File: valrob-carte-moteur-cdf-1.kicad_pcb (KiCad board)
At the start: 2 copper layers, 63 x 50 mm, 85 parts, among them J1 USB_C_Receptacle_USB2.0_14P, J2 Conn_01x02, J3 Conn_01x02, J4 Conn_01x04_Pin, J5 Conn_01x08, J6 Conn_01x02, J7 Conn_01x02, J8 Conn_01x08, SW1 SW_Push, SW2 SW_Push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

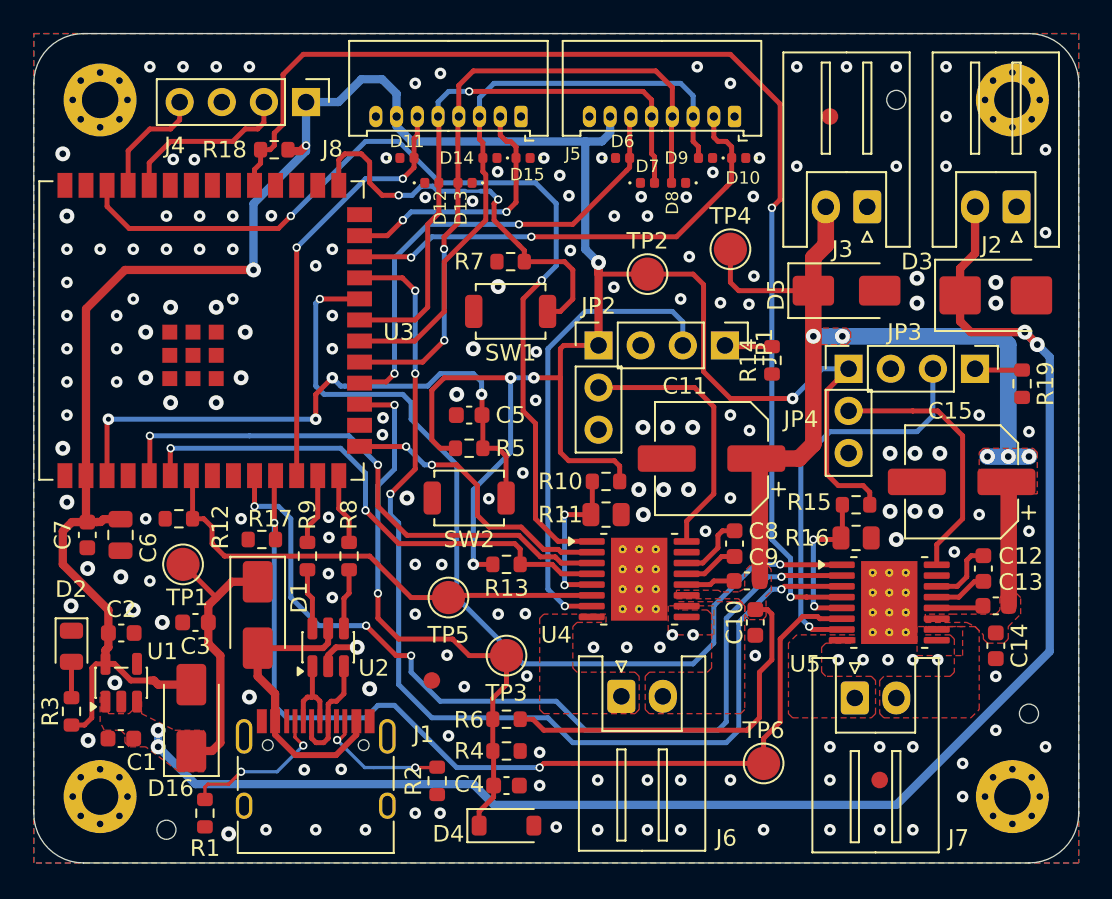
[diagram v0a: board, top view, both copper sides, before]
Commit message: pcb: add silkscreen bling
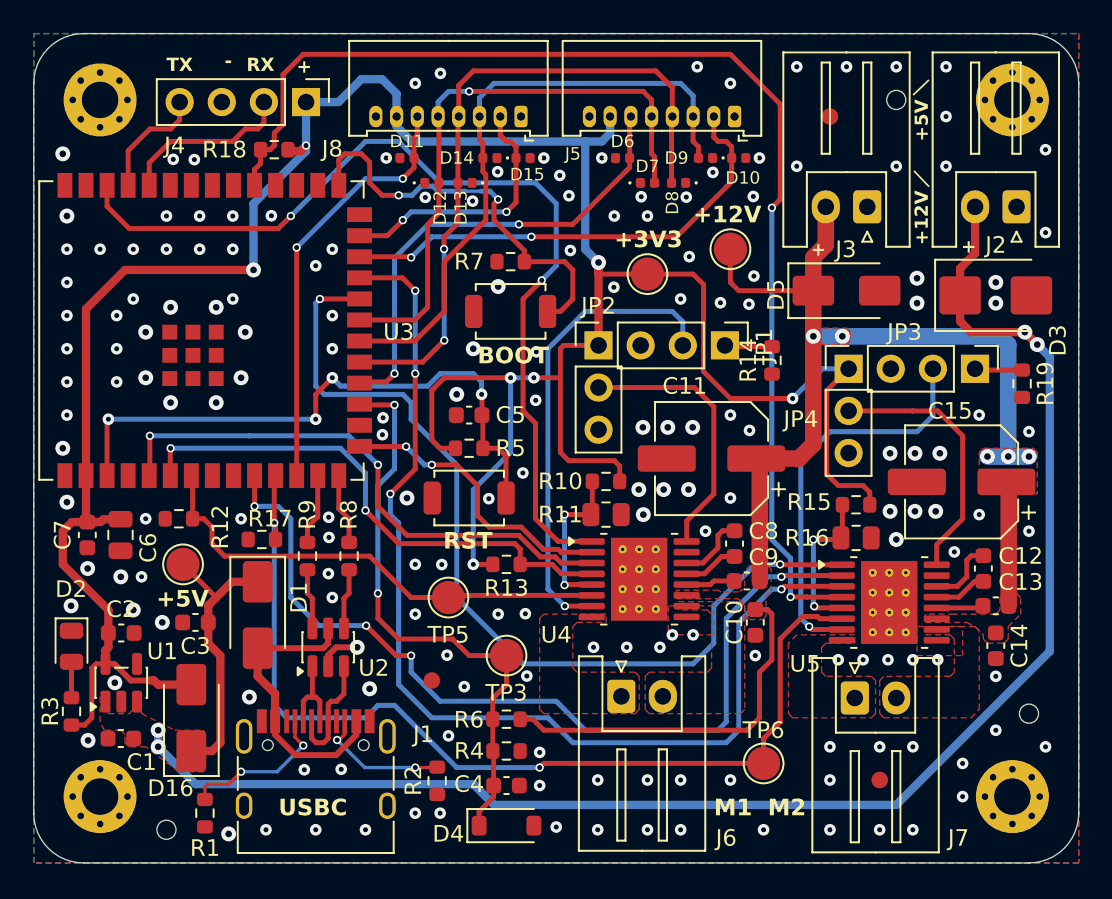
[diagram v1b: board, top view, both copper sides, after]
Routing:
- net GND: vias 183 -> 179
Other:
- board text added: "+"
- board text added: "+12V"
- board text added: "+3V3"
- board text added: "+5V"
- board text added: "-"
- board text added: ">10A"
- board text added: "ALERT1"
- board text added: "ALERT2"
- board text added: "BOOT"
- board text added: "CS0"
- board text added: "CS1"
- board text added: "Carte moteur CDF 1"
- board text added: "GND"
- board text added: "ICHOPPING"
- board text added: "M1"
- board text added: "M2"
- board text added: "MISO"
- board text added: "MOSI"
- board text added: "N"
- board text added: "PH/EN"
- board text added: "PWM"
- board text added: "RST"
- board text added: "RX"
- board text added: "Rev 01"
- board text added: "SCLK"
- board text added: "TX"
- board text added: "USBC"
- board text added: "Valrobotik 2025-11"
- board text added: "Y"

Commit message: add spare gpios
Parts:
- added J9: Conn_01x04_Pin, Connector_PinHeader_2.54mm:PinHeader_1x04_P2.54mm_Vertical, F.Cu at (99.4, 89.5)
- moved R18 29.4 mm to (126.8, 94.8), turned to -90 degrees
- moved J4 2.13 mm to (99.4, 87.0)
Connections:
- C5 pad 1: /CHIP_PU -> GND
- C5 pad 2: GND -> /CHIP_PU
- U3 pad 32: unconnected-(U3-MTCK/GPIO39/CLK_OUT3/SUBSPICS1-Pad32) -> Net-(J9-Pin_1)
- U3 pad 33: unconnected-(U3-MTDO/GPIO40/CLK_OUT2-Pad33) -> Net-(J9-Pin_2)
- U3 pad 34: unconnected-(U3-MTDI/GPIO41/CLK_OUT1-Pad34) -> Net-(J9-Pin_3)
- U3 pad 35: unconnected-(U3-MTMS/GPIO42-Pad35) -> Net-(J9-Pin_4)
- U4 pad 17: GND -> (no net)
- U5 pad 17: GND -> (no net)
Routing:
- net Net-(J9-Pin_1): track 0.00 -> 7.89 mm
- net Net-(J9-Pin_2): track 0.00 -> 6.63 mm
- net Net-(J9-Pin_3): track 0.00 -> 5.96 mm
- net Net-(J9-Pin_4): track 0.00 -> 4.84 mm
- net +3V3: track 169.4 -> 173.9 mm, vias 7 -> 6
- net /U0RXD: track 10.5 -> 12.7 mm
- net /U0TXD: track 7.04 -> 9.20 mm
- net /DC Driver 2/~{FAULT}: track 72.9 -> 72.2 mm
- net GND: vias 179 -> 177
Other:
- board text added: "39"
- board text added: "40"
- board text added: "41"
- board text added: "42"
- board text added: "ENCODER1"
- board text added: "ENCODER2"
- board text added: "GPIO"
- board text added: "UART"

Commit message: pcb(silkscreen): add JLC order number placeholder
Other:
- board text added: "JLCJLCJLCJLC"
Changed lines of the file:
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@@
+		)
+	)
+	(gr_text "JLCJLCJLCJLC"
+		(at 98.25 112.25 0)
+		(layer "B.SilkS")
+		(effects
+			(font
+				(size 1 1)
+				(thickness 0.1)
+			)
+			(justify left bottom mirror)
 		)
 	)

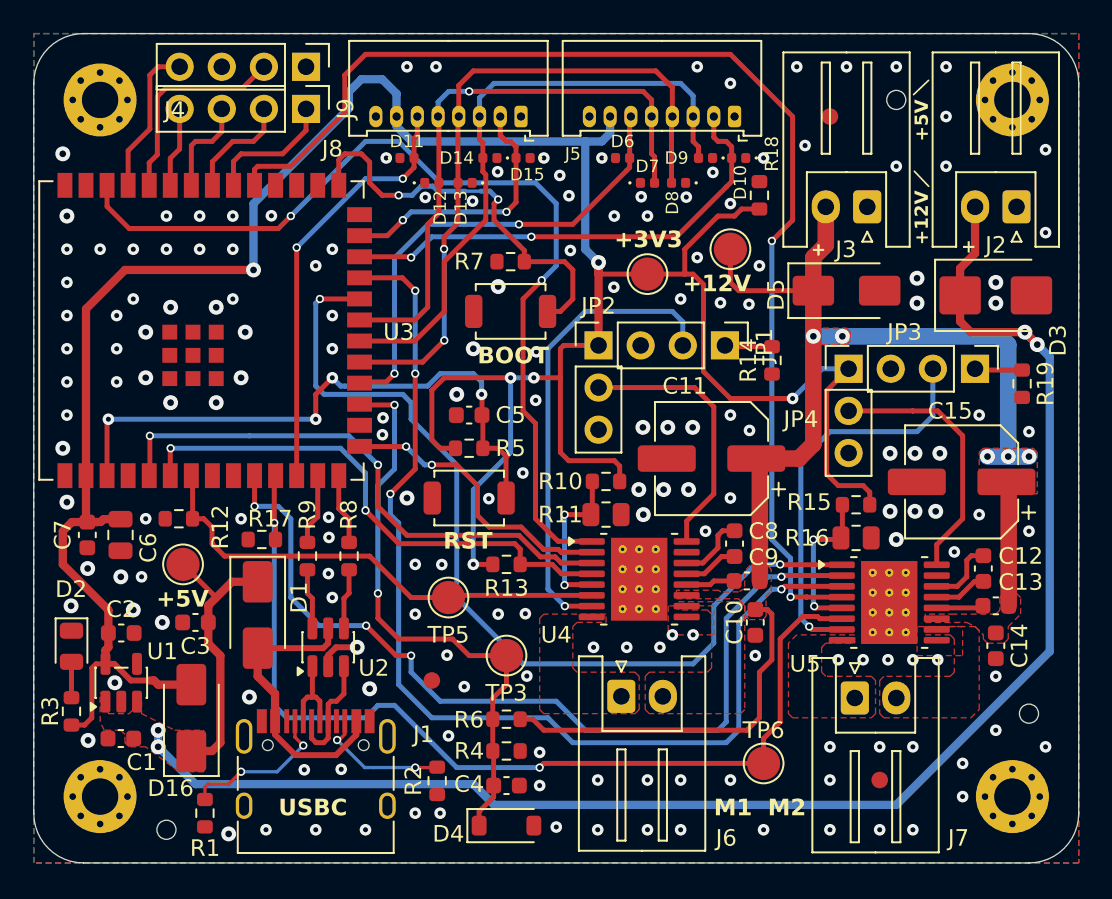
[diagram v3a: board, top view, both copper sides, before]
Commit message: pcb: run and fix DRC
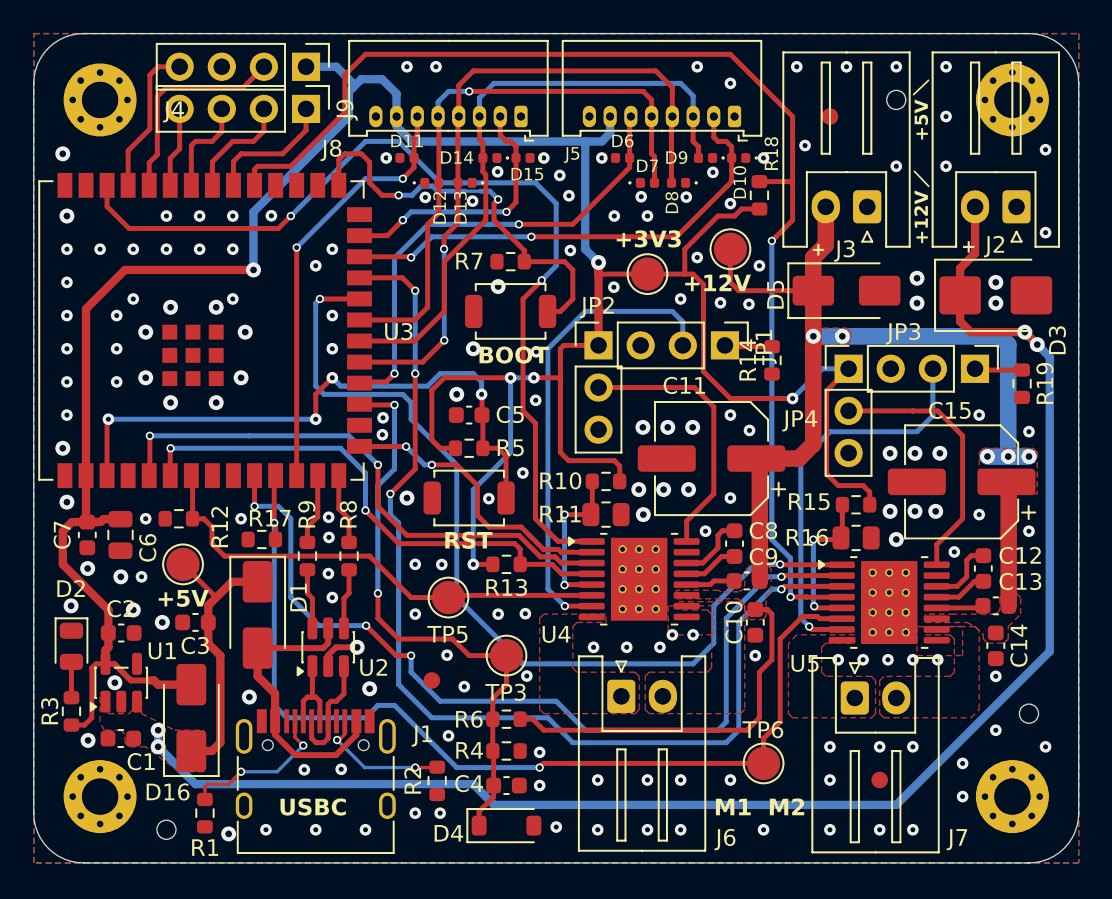
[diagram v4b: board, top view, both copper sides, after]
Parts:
- turned C5 to 0 degrees
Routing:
- net +3V3: track 173.9 -> 177.4 mm
- net /DC Driver 2/~{FAULT}: track 72.2 -> 74.2 mm
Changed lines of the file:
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@@
 			(at -1 -1.8)
 			(size 0.5 0.5)
-			(drill 0.2)
+			(drill 0.3)
 			(property pad_prop_heatsink)
 			(layers "*.Cu")
@@
 			(at -1 -0.6)
 			(size 0.5 0.5)
-			(drill 0.2)
+			(drill 0.3)
 			(property pad_prop_heatsink)
 			(layers "*.Cu")
@@
 			(at -1 0.6)
 			(size 0.5 0.5)
-			(drill 0.2)
+			(drill 0.3)
 			(property pad_prop_heatsink)
 			(layers "*.Cu")
@@
 			(at -1 1.8)
 			(size 0.5 0.5)
-			(drill 0.2)
+			(drill 0.3)
 			(property pad_prop_heatsink)
 			(layers "*.Cu")
@@
 			(at 0 -1.8)
 			(size 0.5 0.5)
-			(drill 0.2)
+			(drill 0.3)
 			(property pad_prop_heatsink)
 			(layers "*.Cu")
@@
 			(at 0 -0.6)
 			(size 0.5 0.5)
-			(drill 0.2)
+			(drill 0.3)
 			(property pad_prop_heatsink)
 			(layers "*.Cu")
@@
 			(at 0 0.6)
 			(size 0.5 0.5)
-			(drill 0.2)
+			(drill 0.3)
 			(property pad_prop_heatsink)
 			(layers "*.Cu")
@@
 			(at 0 1.8)
 			(size 0.5 0.5)
-			(drill 0.2)
+			(drill 0.3)
 			(property pad_prop_heatsink)
 			(layers "*.Cu")
@@
 			(at 1 -1.8)
 			(size 0.5 0.5)
-			(drill 0.2)
+			(drill 0.3)
 			(property pad_prop_heatsink)
 			(layers "*.Cu")
@@
 			(at 1 -0.6)
 			(size 0.5 0.5)
-			(drill 0.2)
+			(drill 0.3)
 			(property pad_prop_heatsink)
 			(layers "*.Cu")
@@
 			(at 1 0.6)
 			(size 0.5 0.5)
-			(drill 0.2)
+			(drill 0.3)
 			(property pad_prop_heatsink)
 			(layers "*.Cu")
@@
 			(at 1 1.8)
 			(size 0.5 0.5)
-			(drill 0.2)
+			(drill 0.3)
 			(property pad_prop_heatsink)
 			(layers "*.Cu")
@@
 		(tags "Diode SMA (DO-214AC)")
 		(property "Reference" "D16"
-			(at -4.25 -1.25 180)
+			(at -4.508165 -1.426515 180)
 			(layer "F.SilkS")
 			(effects
@@
 			(at -1 -1.8)
 			(size 0.5 0.5)
-			(drill 0.2)
+			(drill 0.3)
 			(property pad_prop_heatsink)
 			(layers "*.Cu")
@@
 			(at -1 -0.6)
 			(size 0.5 0.5)
-			(drill 0.2)
+			(drill 0.3)
 			(property pad_prop_heatsink)
 			(layers "*.Cu")
@@
 			(at -1 0.6)
 			(size 0.5 0.5)
-			(drill 0.2)
+			(drill 0.3)
 			(property pad_prop_heatsink)
 			(layers "*.Cu")
@@
 			(at -1 1.8)
 			(size 0.5 0.5)
-			(drill 0.2)
+			(drill 0.3)
 			(property pad_prop_heatsink)
 			(layers "*.Cu")
@@
 			(at 0 -1.8)
 			(size 0.5 0.5)
-			(drill 0.2)
+			(drill 0.3)
 			(property pad_prop_heatsink)
 			(layers "*.Cu")
@@
 			(at 0 -0.6)
 			(size 0.5 0.5)
-			(drill 0.2)
+			(drill 0.3)
 			(property pad_prop_heatsink)
 			(layers "*.Cu")
@@
 			(at 0 0.6)
 			(size 0.5 0.5)
-			(drill 0.2)
+			(drill 0.3)
 			(property pad_prop_heatsink)
 			(layers "*.Cu")
@@
 			(at 0 1.8)
 			(size 0.5 0.5)
-			(drill 0.2)
+			(drill 0.3)
 			(property pad_prop_heatsink)
 			(layers "*.Cu")
@@
 			(at 1 -1.8)
 			(size 0.5 0.5)
-			(drill 0.2)
+			(drill 0.3)
 			(property pad_prop_heatsink)
 			(layers "*.Cu")
@@
 			(at 1 -0.6)
 			(size 0.5 0.5)
-			(drill 0.2)
+			(drill 0.3)
 			(property pad_prop_heatsink)
 			(layers "*.Cu")
@@
 			(at 1 0.6)
 			(size 0.5 0.5)
-			(drill 0.2)
+			(drill 0.3)
 			(property pad_prop_heatsink)
 			(layers "*.Cu")
@@
 			(at 1 1.8)
 			(size 0.5 0.5)
-			(drill 0.2)
+			(drill 0.3)
 			(property pad_prop_heatsink)
 			(layers "*.Cu")
@@
 	(footprint "Capacitor_SMD:C_0603_1608Metric"
 		(layer "F.Cu")
-		(at 109.25 108 180)
+		(at 109.25 108)
 		(descr "Capacitor SMD 0603 (1608 Metric), square (rectangular) end terminal, IPC-7351 nominal, (Body size source: IPC-SM-782 page 76, https://www.pcb-3d.com/wordpress/wp-content/uploads/ipc-sm-782a_amendment_1_and_2.pdf), generated with kicad-footprint-generator")
 		(tags "capacitor")
 		(property "Reference" "C5"
-			(at -2.5 0 0)
+			(at 2.5 0 0)
 			(layer "F.SilkS")
 			(effects
@@
 		)
 		(property "Manufacturer" "Samsung Electro-Mechanics "
-			(at 0 0 180)
+			(at 0 0 0)
 			(unlocked yes)
 			(layer "F.Fab")
@@
 		)
 		(property "Manufacturer Part Number" "CL10A105KB8NNNC"
-			(at 0 0 180)
+			(at 0 0 0)
 			(unlocked yes)
 			(layer "F.Fab")
@@
 		)
 		(property "Basic" "Y"
-			(at 0 0 180)
+			(at 0 0 0)
 			(unlocked yes)
 			(layer "F.Fab")
@@
 		)
 		(property "JLCPCB Part #" "C15849"
-			(at 0 0 180)
+			(at 0 0 0)
 			(unlocked yes)
 			(layer "F.Fab")
@@
 		(attr smd)
 		(fp_line
-			(start -0.14058 0.51)
-			(end 0.14058 0.51)
+			(start -0.14058 -0.51)
+			(end 0.14058 -0.51)
 			(stroke
 				(width 0.12)
@@
 		)
 		(fp_line
-			(start -0.14058 -0.51)
-			(end 0.14058 -0.51)
+			(start -0.14058 0.51)
+			(end 0.14058 0.51)
 			(stroke
 				(width 0.12)
@@
 		)
 		(fp_line
-			(start 1.48 0.73)
-			(end -1.48 0.73)
+			(start -1.48 -0.73)
+			(end 1.48 -0.73)
 			(stroke
 				(width 0.05)
@@
 		)
 		(fp_line
-			(start 1.48 -0.73)
-			(end 1.48 0.73)
+			(start -1.48 0.73)
+			(end -1.48 -0.73)
 			(stroke
 				(width 0.05)
@@
 		)
 		(fp_line
-			(start -1.48 0.73)
-			(end -1.48 -0.73)
+			(start 1.48 -0.73)
+			(end 1.48 0.73)
 			(stroke
 				(width 0.05)
@@
 		)
 		(fp_line
-			(start -1.48 -0.73)
-			(end 1.48 -0.73)
+			(start 1.48 0.73)
+			(end -1.48 0.73)
 			(stroke
 				(width 0.05)
@@
 		)
 		(fp_line
-			(start 0.8 0.4)
-			(end -0.8 0.4)
+			(start -0.8 -0.4)
+			(end 0.8 -0.4)
 			(stroke
 				(width 0.1)
@@
 		)
 		(fp_line
-			(start 0.8 -0.4)
-			(end 0.8 0.4)
+			(start -0.8 0.4)
+			(end -0.8 -0.4)
 			(stroke
 				(width 0.1)
@@
 		)
 		(fp_line
-			(start -0.8 0.4)
-			(end -0.8 -0.4)
+			(start 0.8 -0.4)
+			(end 0.8 0.4)
 			(stroke
 				(width 0.1)
@@
 		)
 		(fp_line
-			(start -0.8 -0.4)
-			(end 0.8 -0.4)
+			(start 0.8 0.4)
+			(end -0.8 0.4)
 			(stroke
 				(width 0.1)
@@
 		)
 		(pad "1" smd roundrect
-			(at -0.775 0 180)
+			(at -0.775 0)
 			(size 0.9 0.95)
 			(layers "F.Cu" "F.Mask" "F.Paste")
@@
 		)
 		(pad "2" smd roundrect
-			(at 0.775 0 180)
+			(at 0.775 0)
 			(size 0.9 0.95)
 			(layers "F.Cu" "F.Mask" "F.Paste")
@@
 	)
 	(segment
-		(start 102 89.5)
-		(end 102 88.5)
+		(start 109.5 117)
+		(end 109.5 112.5)
+		(width 0.3)
+		(layer "B.Cu")
+		(net 3)
+	)
+	(segment
+		(start 101.25 87)
+		(end 99.41614 87)
 		(width 0.5)
 		(layer "B.Cu")
@@
 	)
 	(segment
-		(start 109.5 117)
-		(end 109.5 112.5)
-		(width 0.3)
+		(start 96.25 99.25)
+		(end 96.25 95.75)
+		(width 0.5)
 		(layer "B.Cu")
 		(net 3)
@@
 	)
 	(segment
-		(start 96.25 95.25)
-		(end 102 89.5)
+		(start 102.75 87.75)
+		(end 104 87.75)
 		(width 0.5)
 		(layer "B.Cu")
@@
 	)
 	(segment
-		(start 102.75 87.75)
-		(end 104 87.75)
+		(start 102 88.5)
+		(end 102.25 88.25)
 		(width 0.5)
 		(layer "B.Cu")
@@
 	)
 	(segment
+		(start 102.25 88.25)
+		(end 102.25 88)
+		(width 0.5)
+		(layer "B.Cu")
+		(net 3)
+	)
+	(segment
 		(start 111.75 110.25)
 		(end 111.75 105.75)
@@
 	)
 	(segment
-		(start 96.25 99.25)
-		(end 96.25 95.25)
+		(start 96.25 95.75)
+		(end 102 90)
 		(width 0.5)
 		(layer "B.Cu")
@@
 	)
 	(segment
-		(start 102 88.5)
+		(start 102 90)
+		(end 102 88.5)
+		(width 0.5)
+		(layer "B.Cu")
+		(net 3)
+	)
+	(segment
+		(start 102.25 88.25)
 		(end 102.75 87.75)
 		(width 0.5)
@@
 	)
 	(segment
+		(start 102.25 88)
+		(end 101.25 87)
+		(width 0.5)
+		(layer "B.Cu")
+		(net 3)
+	)
+	(segment
 		(start 104.875 90)
 		(end 104.875 90.595768)
@@
 	)
 	(segment
+		(start 128.675 93.925)
+		(end 128.75 94)
+		(width 0.3)
+		(layer "F.Cu")
+		(net 50)
+	)
+	(segment
 		(start 96.31 93.19)
 		(end 96.5 93)
@@
 	)
 	(segment
+		(start 128.75 90)
+		(end 128.75 94)
+		(width 0.3)
+		(layer "F.Cu")
+		(net 50)
+	)
+	(segment
 		(start 101.75 89.75)
 		(end 101.75 87.5)
@@
 	)
 	(segment
-		(start 128.75 90)
+		(start 128.75 94)
 		(end 128.75 96.25)
 		(width 0.3)
@@
 		(width 0.3)
 		(layer "F.Cu")
+		(net 50)
+	)
+	(segment
+		(start 126.75 93.925)
+		(end 128.675 93.925)
+		(width 0.3)
+		(layer "F.Cu")

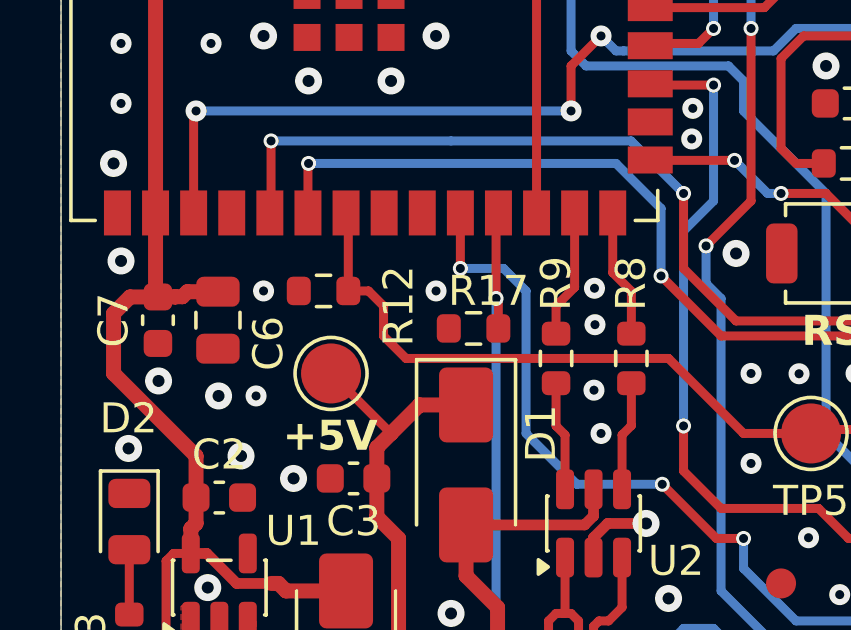
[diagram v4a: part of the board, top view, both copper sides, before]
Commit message: pcb: add company logo to back
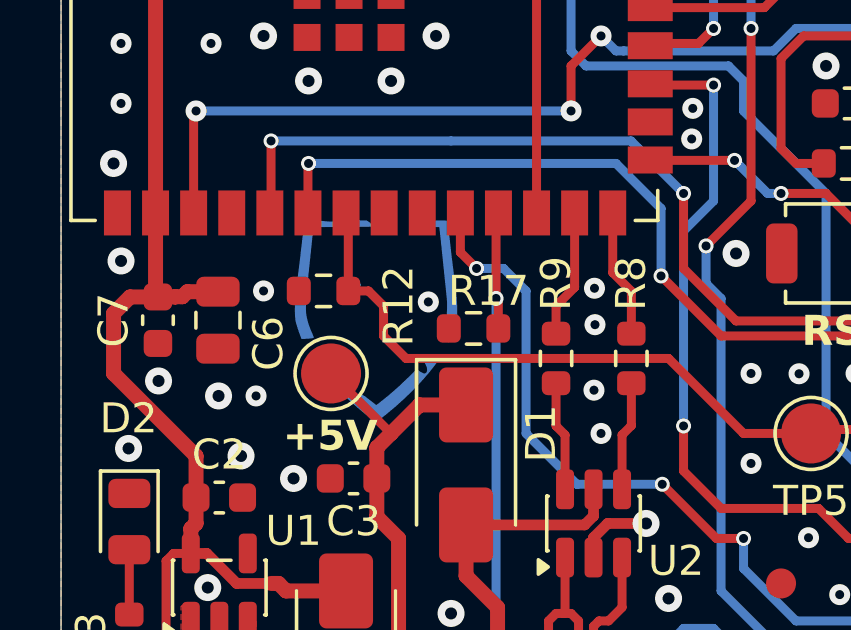
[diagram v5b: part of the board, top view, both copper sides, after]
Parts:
- added G***: LOGO, LOGO, B.Cu at (93.5, 114.5)
- added G*** (x2): LOGO, LOGO, B.Cu at (93.5, 114.6)
